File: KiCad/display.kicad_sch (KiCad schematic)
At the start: 32 parts, among them IC1 TPS22916CNYFPR, IC2 TPS22916CNYFPR, IC3 R1200N001A-TR-FE, J3 Conn_01x34_NHD_18, U6 MCP1700x-250xxTT

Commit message: PCB Layout V0.1 with errors
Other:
- company: ETH Zurich: Center for Project Based Learning -> ETH Zürich: Center for Project Based Learning
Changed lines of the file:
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@@
 		(date "2026-03-09")
 		(rev "0.0.2")
-		(company "ETH Zurich: Center for Project Based Learning")
+		(company "ETH Zürich: Center for Project Based Learning")
 	)
 	(rectangle

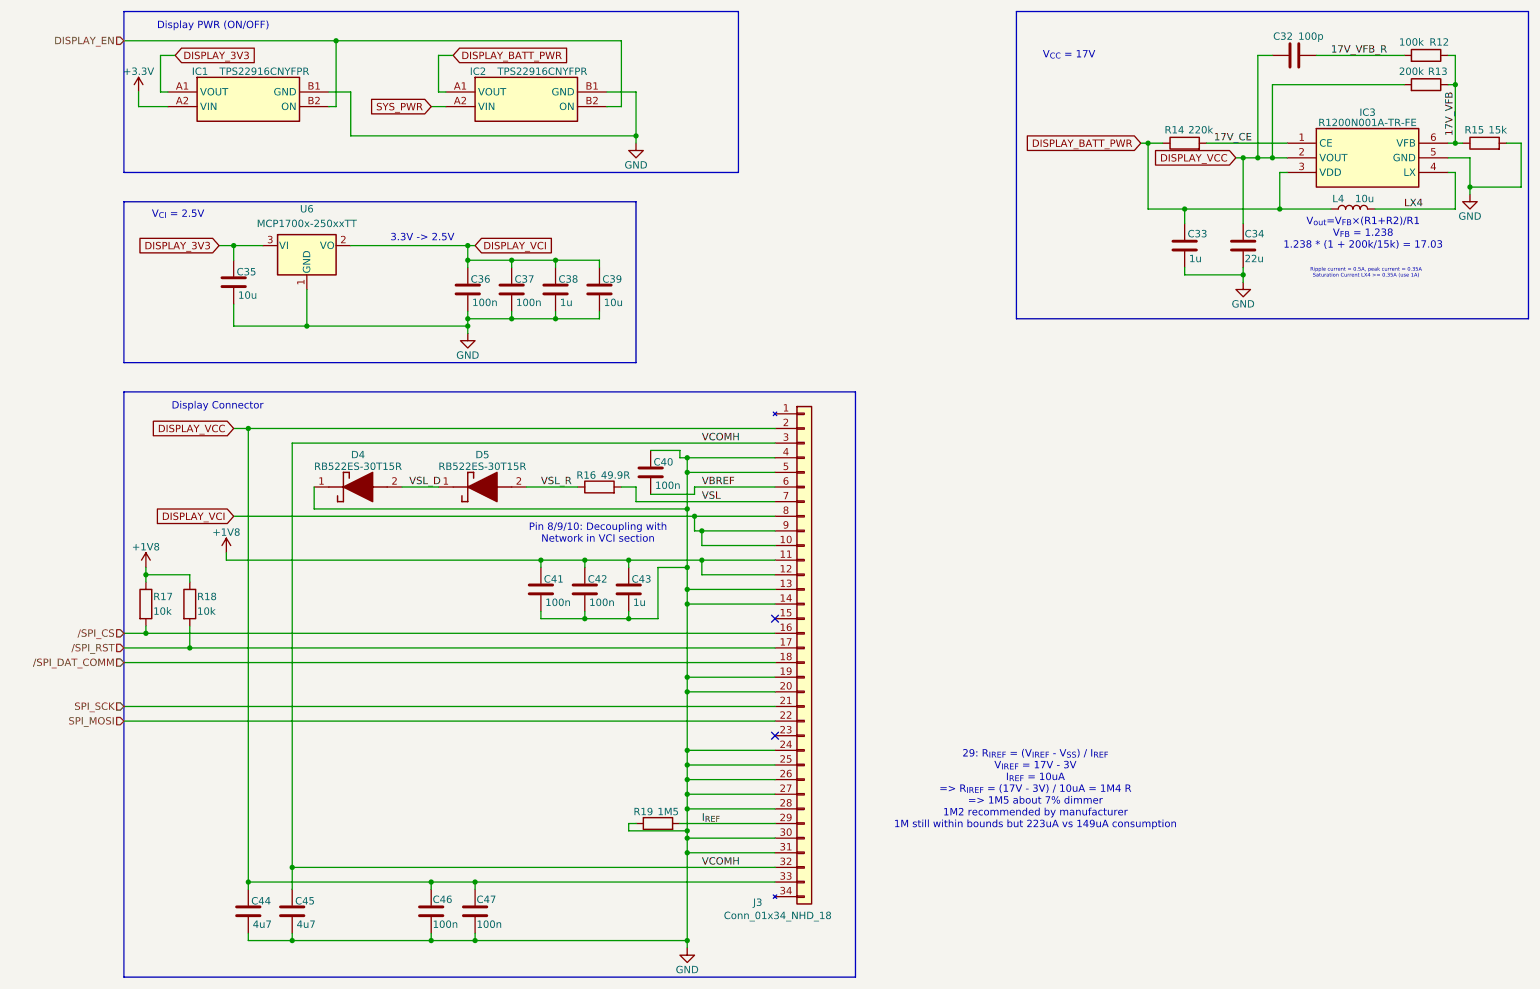
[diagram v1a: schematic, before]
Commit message: Update Libs for connector etc
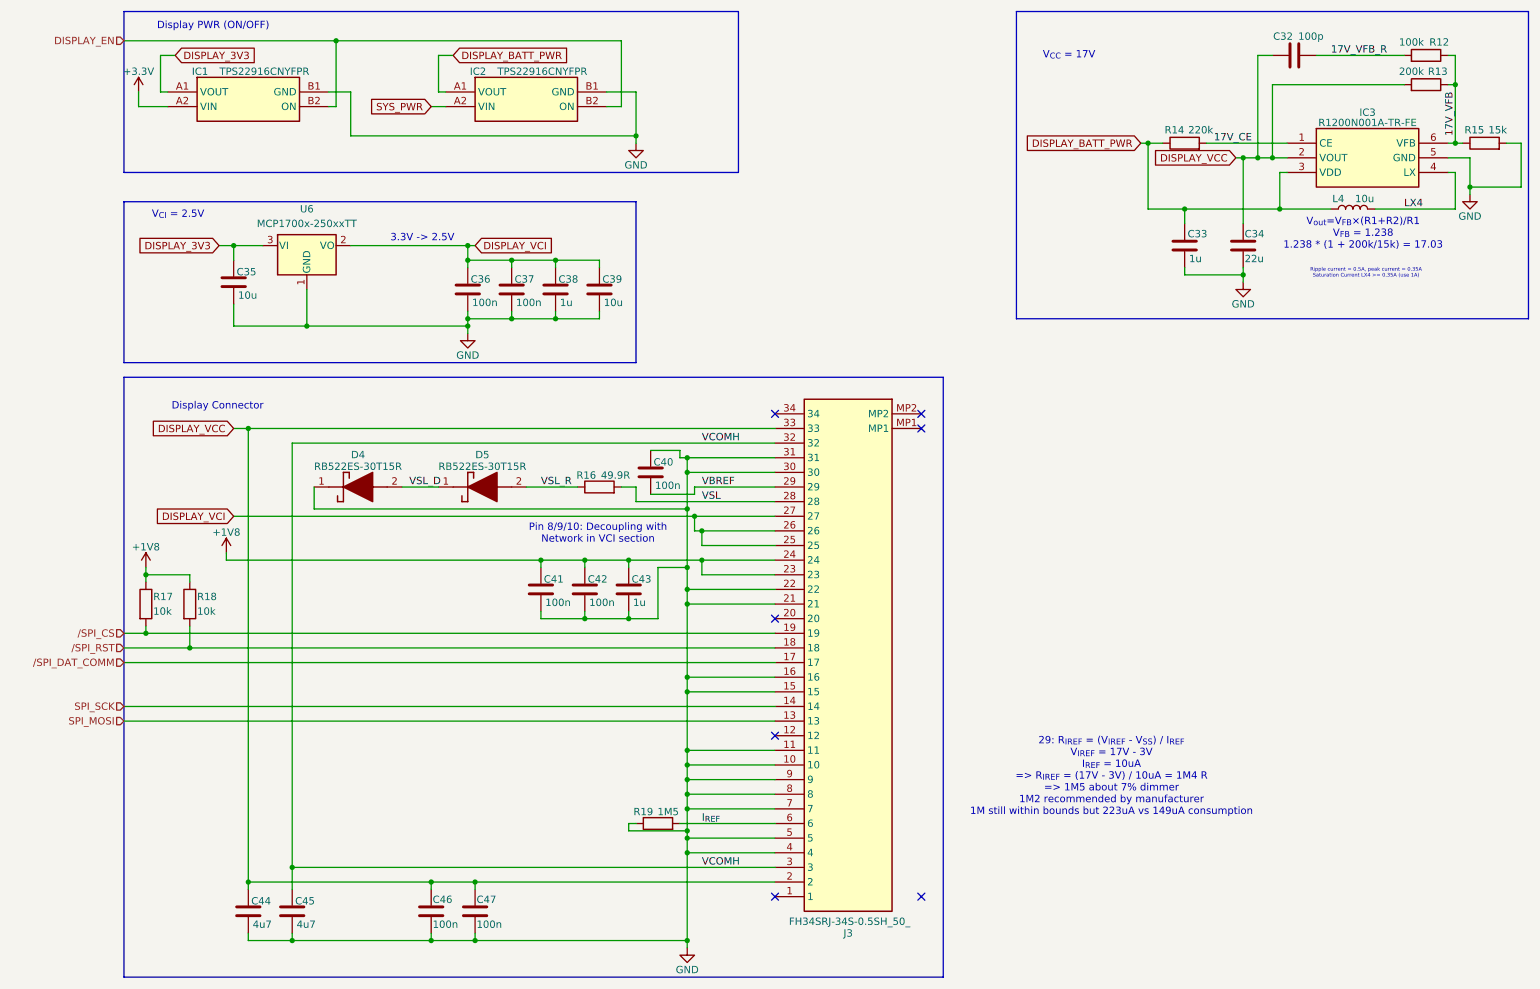
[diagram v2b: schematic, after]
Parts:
- removed J3: Conn_01x34_NHD_18, Connector_FFC-FPC:TE_3-1734839-4_1x34-1MP_P0.5mm_Horizontal, symbol NHD-18:Conn_01x34_NHD_18
- added J3: FH34SRJ-34S-0.5SH_50_, FCC FPC 34Pin:FH34SRJ34S05SH50, symbol FCC FPC Connector 34Pin:FH34SRJ-34S-0.5SH_50_
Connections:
- net +1V8: now also J3.23, J3.24
- net DISPLAY_VCC: now also J3.2, J3.33
- net DISPLAY_VCI: now also J3.25, J3.26, J3.27
- net GND: now also J3.10, J3.11, J3.15, J3.16, J3.21, J3.22, J3.30, J3.31, J3.4, J3.5, J3.7, J3.8, J3.9
- net I_{REF}: now also J3.6
- net SPI_MOSI: now also J3.13
- net SPI_SCK: now also J3.14
- net VBREF: now also J3.29
- net VCOMH: now also J3.3, J3.32
- net VSL: now also J3.28
- net /SPI_CS: now also J3.19
- net /SPI_DAT_COMM: now also J3.17
- net /SPI_RST: now also J3.18
- no-connect marks 2 -> 7
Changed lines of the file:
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@@
 	)
 	(rectangle
-		(start 30.48 88.9)
-		(end 157.48 190.5)
+		(start 30.48 86.36)
+		(end 172.72 190.5)
 		(stroke
 			(width 0)
@@
 	(text "29: R_{IREF} = (V_{IREF} - V_{SS}) / I_{REF}\nV_{IREF} = 17V - 3V\nI_{REF} = 10uA\n=> R_{IREF} = (17V - 3V) / 10uA = 1M4 R\n=> 1M5 about 7% dimmer\n1M2 recommended by manufacturer\n1M still within bounds but 223uA vs 149uA consumption"
 		(exclude_from_sim no)
-		(at 188.722 157.988 0)
+		(at 201.93 155.702 0)
 		(effects
 			(font
@@
 	)
 	(no_connect
+		(at 143.51 92.71)
+	)
+	(no_connect
 		(at 143.51 128.27)
 	)
 	(no_connect
+		(at 168.91 176.53)
+	)
+	(no_connect
+		(at 143.51 176.53)
+	)
+	(no_connect
 		(at 143.51 148.59)
 	)
+	(no_connect
+		(at 168.91 92.71)
+	)
+	(no_connect
+		(at 168.91 95.25)
+	)
 	(wire
 		(pts
@@
 	)
 	(symbol
-		(lib_id "NHD-18:Conn_01x34_NHD_18")
-		(at 148.59 133.35 0)
-		(unit 1)
-		(exclude_from_sim no)
-		(in_bom yes)
-		(on_board yes)
-		(dnp no)
-		(property "Reference" "J3"
-			(at 139.7 177.546 0)
-			(effects
-				(font
-					(size 1.27 1.27)
-				)
-				(justify left)
-			)
-		)
-		(property "Value" "Conn_01x34_NHD_18"
-			(at 134.62 179.832 0)
-			(effects
-				(font
-					(size 1.27 1.27)
-				)
-				(justify left)
-			)
-		)
-		(property "Footprint" "Connector_FFC-FPC:TE_3-1734839-4_1x34-1MP_P0.5mm_Horizontal"
-			(at 148.59 133.35 0)
-			(effects
-				(font
-					(size 1.27 1.27)
-				)
-				(hide yes)
-			)
-		)
-		(property "Datasheet" "~"
-			(at 148.59 133.35 0)
-			(effects
-				(font
-					(size 1.27 1.27)
-				)
-				(hide yes)
-			)
-		)
-		(property "Description" "Generic connector, single row, 01x34, script generated (kicad-library-utils/schlib/autogen/connector/)"
-			(at 148.59 133.35 0)
-			(effects
-				(font
-					(size 1.27 1.27)
-				)
-				(hide yes)
-			)
-		)
-		(pin "5"
-		)
-		(pin "6"
-		)
-		(pin "10"
-		)
-		(pin "8"
-		)
-		(pin "11"
-		)
-		(pin "7"
-		)
-		(pin "15"
-		)
-		(pin "12"
-		)
-		(pin "14"
-		)
-		(pin "13"
-		)
-		(pin "3"
-		)
-		(pin "2"
-		)
-		(pin "4"
-		)
-		(pin "9"
-		)
-		(pin "1"
-		)
-		(pin "17"
-		)
-		(pin "16"
-		)
-		(pin "18"
-		)
-		(pin "22"
-		)
-		(pin "19"
-		)
-		(pin "23"
-		)
-		(pin "21"
-		)
-		(pin "20"
-		)
-		(pin "24"
-		)
-		(pin "34"
-		)
-		(pin "32"
-		)
-		(pin "33"
-		)
-		(pin "30"
-		)
-		(pin "31"
-		)
-		(pin "28"
-		)
-		(pin "29"
-		)
-		(pin "26"
-		)
-		(pin "27"
-		)
-		(pin "25"
-		)
-		(instances
-			(project ""
-				(path "/643c756f-a801-466b-9148-7370ee6a5e00/603cffac-84d5-485b-bf95-e3987997ef84"
-					(reference "J3")
-					(unit 1)
-				)
-			)
-		)
-	)
-	(symbol
 		(lib_id "TPS22916CNYFPR:TPS22916CNYFPR")
 		(at 86.36 36.83 0)
@@
 					(unit 1)
 				)
+			)
+		)
+	)
+	(symbol
+		(lib_id "FCC FPC Connector 34Pin:FH34SRJ-34S-0.5SH_50_")
+		(at 168.91 92.71 0)
+		(mirror y)
+		(unit 1)
+		(exclude_from_sim no)
+		(in_bom yes)
+		(on_board yes)
+		(dnp no)
+		(property "Reference" "J3"
+			(at 156.21 182.88 0)
+			(effects
+				(font
+					(size 1.27 1.27)
+				)
+			)
+		)
+		(property "Value" "FH34SRJ-34S-0.5SH_50_"
+			(at 156.464 180.848 0)
+			(effects
+				(font
+					(size 1.27 1.27)
+				)
+			)
+		)
+		(property "Footprint" "FCC FPC 34Pin:FH34SRJ34S05SH50"
+			(at 147.32 187.63 0)
+			(effects
+				(font
+					(size 1.27 1.27)
+				)
+				(justify left top)
+				(hide yes)
+			)
+		)
+		(property "Datasheet" "https://www.hirose.com/en/product/document?clcode=CL0580-1261-9-50&productname=FH34SRJ-34S-0.5SH(50)&series=FH34SRJ&documenttype=2DDrawing&lang=en&documentid=0001483059"
+			(at 147.32 287.63 0)
+			(effects
+				(font
+					(size 1.27 1.27)
+				)
+				(justify left top)
+				(hide yes)
+			)
+		)
+		(property "Description" "FFC & FPC Connectors 34POS .5MM"
+			(at 168.91 92.71 0)
+			(effects
+				(font
+					(size 1.27 1.27)
+				)
+				(hide yes)
+			)
+		)
+		(property "Height" "1.1"
+			(at 147.32 487.63 0)
+			(effects
+				(font
+					(size 1.27 1.27)
+				)
+				(justify left top)
+				(hide yes)
+			)
+		)
+		(property "Mouser Part Number" "798-FH34SRJ34S05SH50"
+			(at 147.32 587.63 0)
+			(effects
+				(font
+					(size 1.27 1.27)
+				)
+				(justify left top)
+				(hide yes)
+			)
+		)
+		(property "Mouser Price/Stock" "https://www.mouser.co.uk/ProductDetail/Hirose-Connector/FH34SRJ-34S-0.5SH50?qs=iyLo5FA4poAumYnqXazWvw%3D%3D"
+			(at 147.32 687.63 0)
+			(effects
+				(font
+					(size 1.27 1.27)
+				)
+				(justify left top)
+				(hide yes)
+			)
+		)
+		(property "Manufacturer_Name" "Hirose"
+			(at 147.32 787.63 0)
+			(effects
+				(font
+					(size 1.27 1.27)
+				)
+				(justify left top)
+				(hide yes)
+			)
+		)
+		(property "Manufacturer_Part_Number" "FH34SRJ-34S-0.5SH(50)"
+			(at 147.32 887.63 0)
+			(effects
+				(font
+					(size 1.27 1.27)
+				)
+				(justify left top)
+				(hide yes)
+			)
+		)
+		(pin "21"
+		)
+		(pin "20"
+		)
+		(pin "6"
+		)
+		(pin "7"
+		)
+		(pin "8"
+		)
+		(pin "9"
+		)
+		(pin "10"
+		)
+		(pin "11"
+		)
+		(pin "12"
+		)
+		(pin "13"
+		)
+		(pin "14"
+		)
+		(pin "15"
+		)
+		(pin "16"
+		)
+		(pin "17"
+		)
+		(pin "18"
+		)
+		(pin "19"
+		)
+		(pin "1"
+		)
+		(pin "2"
+		)
+		(pin "3"
+		)
+		(pin "4"
+		)
+		(pin "5"
+		)
+		(pin "MP2"
+		)
+		(pin "MP1"
+		)
+		(pin "34"
+		)
+		(pin "33"
+		)
+		(pin "32"
+		)
+		(pin "31"
+		)
+		(pin "30"
+		)
+		(pin "29"
+		)
+		(pin "28"
+		)
+		(pin "27"
+		)
+		(pin "26"
+		)
+		(pin "25"
+		)
+		(pin "24"
+		)
+		(pin "23"
+		)
+		(pin "22"
+		)
+		(instances
+			(project ""
+				(path "/643c756f-a801-466b-9148-7370ee6a5e00/603cffac-84d5-485b-bf95-e3987997ef84"
+					(reference "J3")
+					(unit 1)
+				)

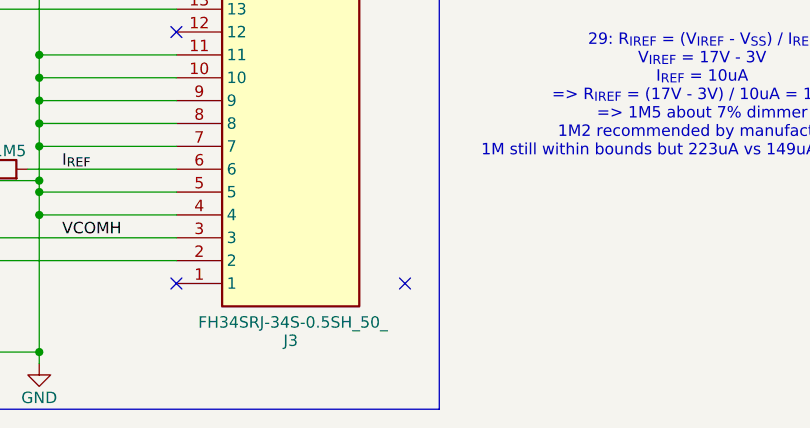
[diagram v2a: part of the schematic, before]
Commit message: V2 beginning with buttons, resistor, ...
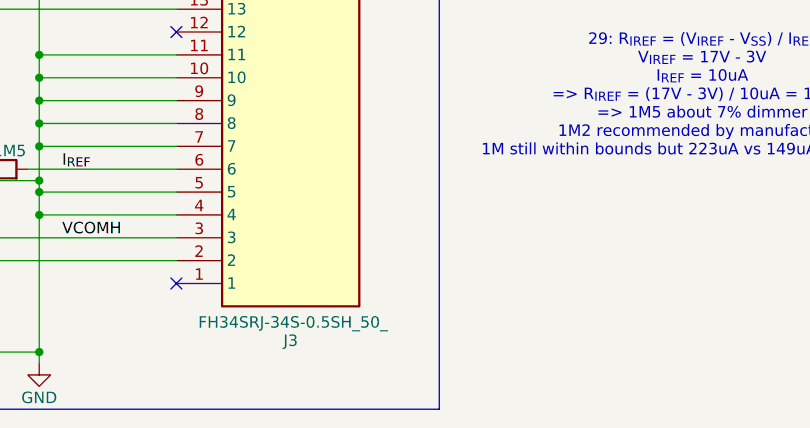
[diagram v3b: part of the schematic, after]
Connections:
- no-connect marks 7 -> 6
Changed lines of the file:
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@@
 	(title_block
 		(title "STDC: Display")
-		(date "2026-03-09")
-		(rev "0.0.2")
+		(date "2026-05-02")
+		(rev "2.0.0")
 		(company "ETH Zürich: Center for Project Based Learning")
 	)
@@
 	)
 	(no_connect
-		(at 168.91 176.53)
-	)
-	(no_connect

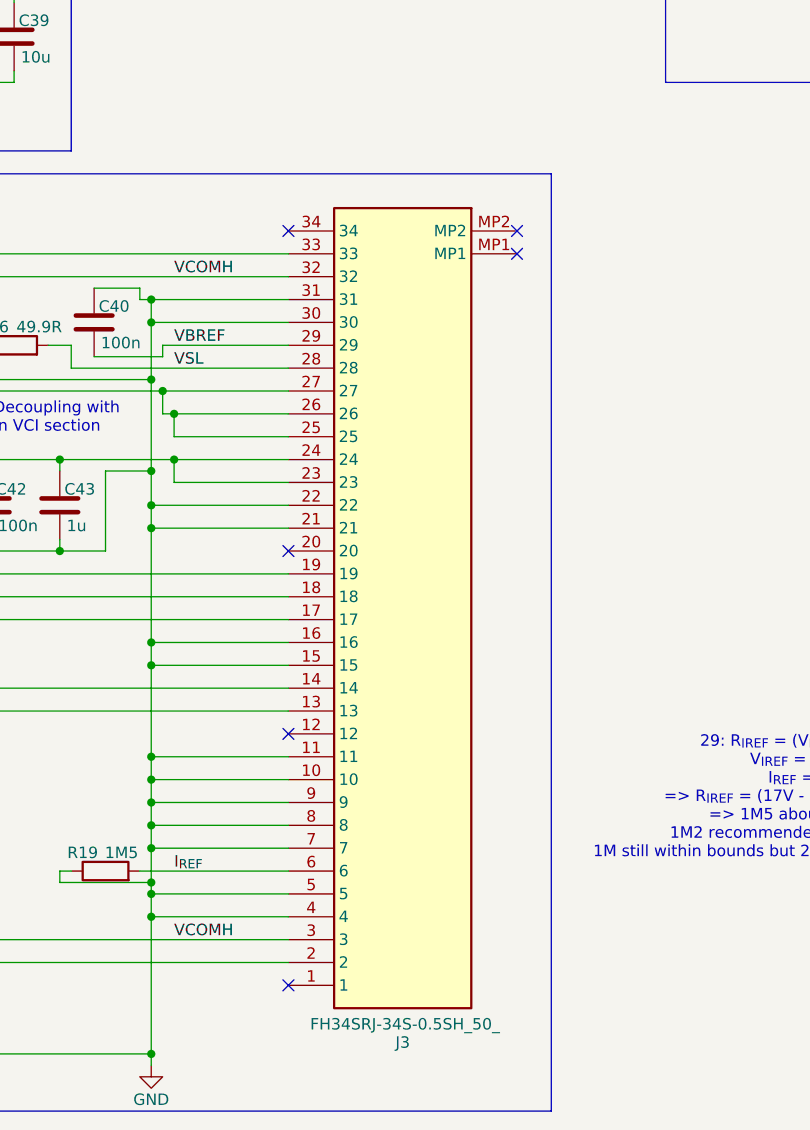
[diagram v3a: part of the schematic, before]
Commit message: Display inverted
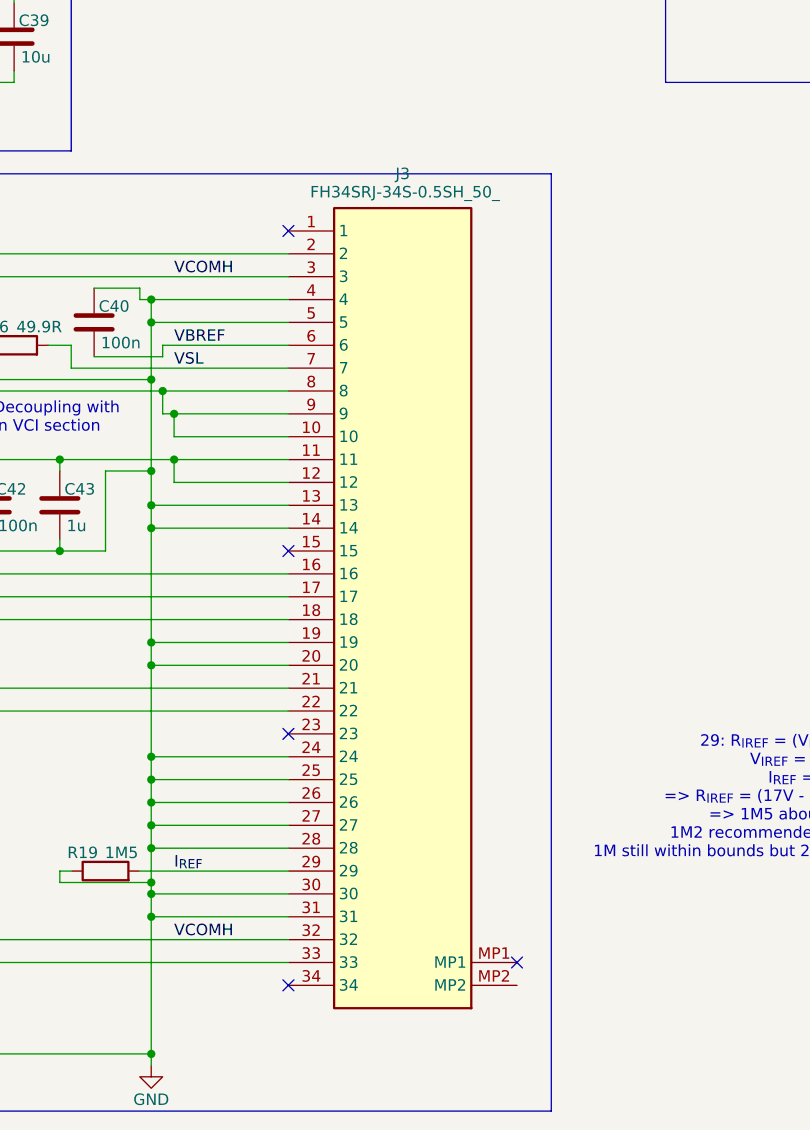
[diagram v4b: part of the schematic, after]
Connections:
- net +1V8: now also J3.11, J3.12; no longer J3.23, J3.24
- net DISPLAY_VCI: now also J3.10, J3.8, J3.9; no longer J3.25, J3.26, J3.27
- net GND: now also J3.13, J3.14, J3.19, J3.20, J3.24, J3.25, J3.26, J3.27, J3.28; no longer J3.10, J3.11, J3.15, J3.16, J3.21, J3.22, J3.7, J3.8, J3.9
- net I_{REF}: now also J3.29; no longer J3.6
- net SPI_MOSI: now also J3.22; no longer J3.13
- net SPI_SCK: now also J3.21; no longer J3.14
- net VBREF: now also J3.6; no longer J3.29
- net VSL: now also J3.7; no longer J3.28
- net /SPI_CS: now also J3.16; no longer J3.19
- net /SPI_DAT_COMM: now also J3.18; no longer J3.17
- net /SPI_RST: now also J3.17; no longer J3.18
- no-connect marks 6 -> 5
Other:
- moved on the sheet: J3
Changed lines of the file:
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@@
 	)
 	(no_connect
-		(at 168.91 92.71)
-	)
-	(no_connect
-		(at 168.91 95.25)
+		(at 168.91 173.99)
 	)
 	(wire
@@
 	(symbol
 		(lib_id "FCC FPC Connector 34Pin:FH34SRJ-34S-0.5SH_50_")
-		(at 168.91 92.71 0)
-		(mirror y)
+		(at 168.91 176.53 180)
 		(unit 1)
 		(exclude_from_sim no)
@@
 		(dnp no)
 		(property "Reference" "J3"
-			(at 156.21 182.88 0)
+			(at 156.21 86.36 0)
 			(effects
 				(font
@@
 		)
 		(property "Value" "FH34SRJ-34S-0.5SH_50_"
-			(at 156.464 180.848 0)
+			(at 156.464 88.392 0)
 			(effects
 				(font
@@
 		)
 		(property "Footprint" "FCC FPC 34Pin:FH34SRJ34S05SH50"
-			(at 147.32 187.63 0)
+			(at 147.32 81.61 0)
 			(effects
 				(font
@@
 		)
 		(property "Datasheet" "https://www.hirose.com/en/product/document?clcode=CL0580-1261-9-50&productname=FH34SRJ-34S-0.5SH(50)&series=FH34SRJ&documenttype=2DDrawing&lang=en&documentid=0001483059"
-			(at 147.32 287.63 0)
+			(at 147.32 -18.39 0)
 			(effects
 				(font
@@
 		)
 		(property "Description" "FFC & FPC Connectors 34POS .5MM"
-			(at 168.91 92.71 0)
+			(at 168.91 176.53 0)
 			(effects
 				(font
@@
 		)
 		(property "Height" "1.1"
-			(at 147.32 487.63 0)
+			(at 147.32 -218.39 0)
 			(effects
 				(font
@@
 		)
 		(property "Mouser Part Number" "798-FH34SRJ34S05SH50"
-			(at 147.32 587.63 0)
+			(at 147.32 -318.39 0)
 			(effects
 				(font
@@
 		)
 		(property "Mouser Price/Stock" "https://www.mouser.co.uk/ProductDetail/Hirose-Connector/FH34SRJ-34S-0.5SH50?qs=iyLo5FA4poAumYnqXazWvw%3D%3D"
-			(at 147.32 687.63 0)
+			(at 147.32 -418.39 0)
 			(effects
 				(font
@@
 		)
 		(property "Manufacturer_Name" "Hirose"
-			(at 147.32 787.63 0)
+			(at 147.32 -518.39 0)
 			(effects
 				(font
@@
 		)
 		(property "Manufacturer_Part_Number" "FH34SRJ-34S-0.5SH(50)"
-			(at 147.32 887.63 0)
+			(at 147.32 -618.39 0)
 			(effects
 				(font
